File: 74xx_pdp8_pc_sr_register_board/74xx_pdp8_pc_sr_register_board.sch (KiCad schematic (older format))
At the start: 33 parts, among them P1 DIL24, P2 DIL24, P3 DIL24, P4 DIL24, P5 DIL24, U1 74HC125, U10 74HC04, U11 74HC163, U12 74HC163, U13 74HC163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

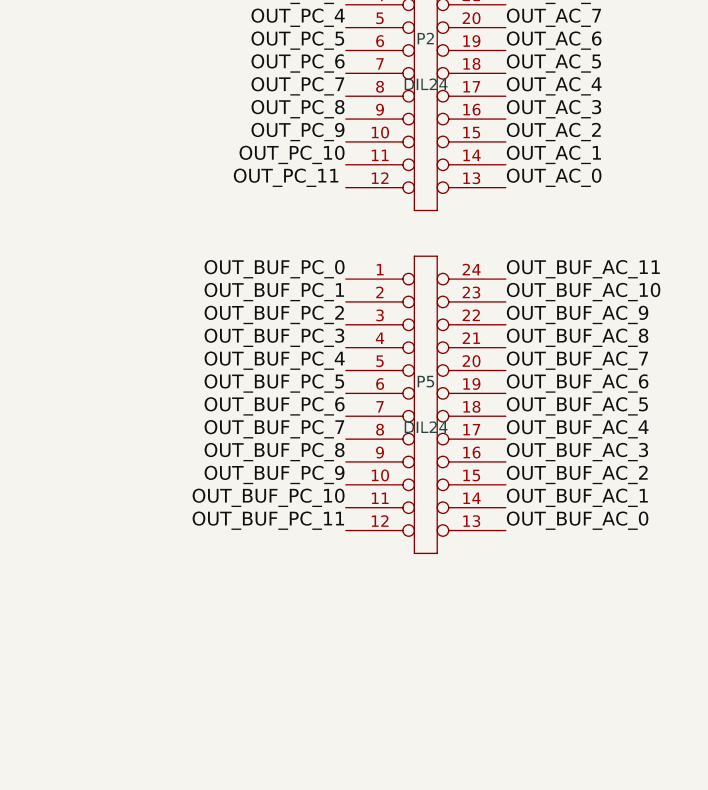
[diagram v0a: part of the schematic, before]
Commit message: Big changes - elected to switch to board interconnections along one long edge only. Boards to connect to backplane via right-angled DIL connectors. Both register boards and register mux boards thusly modified.
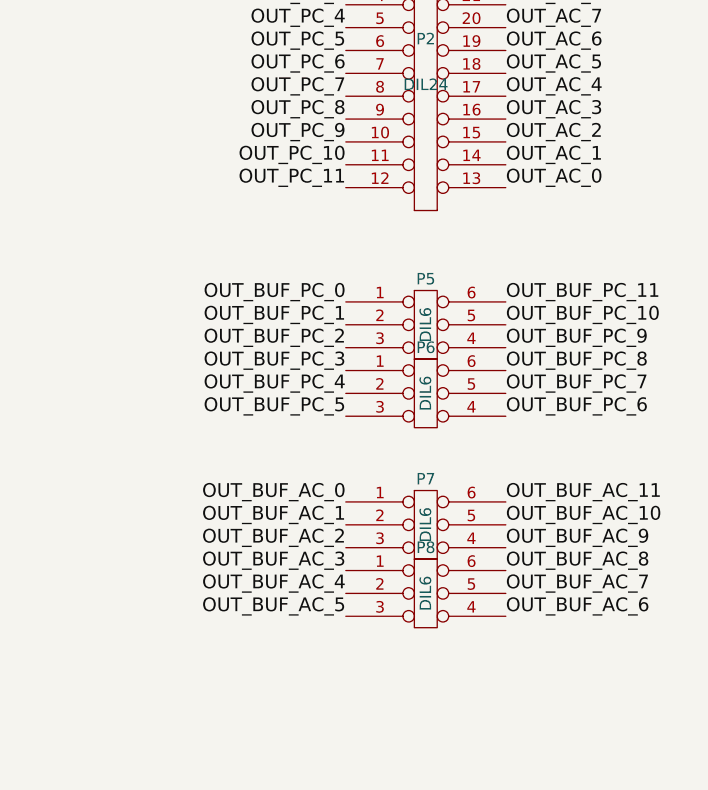
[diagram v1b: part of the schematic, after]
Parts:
- removed P5: DIL24, Socket_Strips:Socket_Strip_Straight_2x12, symbol DIL24
- added P5, P6, P7, P8: DIL6, Socket_Strips:Socket_Strip_Straight_2x03, symbol DIL6
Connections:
- net OUT_BUF_AC_0: now also P7.1 (P1)
- net OUT_BUF_AC_1: now also P7.2 (P2)
- net OUT_BUF_AC_10: now also P7.5 (P5)
- net OUT_BUF_AC_11: now also P7.6 (P6)
- net OUT_BUF_AC_2: now also P7.3 (P3)
- net OUT_BUF_AC_3: now also P8.1 (P1)
- net OUT_BUF_AC_4: now also P8.2 (P2)
- net OUT_BUF_AC_5: now also P8.3 (P3)
- net OUT_BUF_AC_6: now also P8.4 (P4)
- net OUT_BUF_AC_7: now also P8.5 (P5)
- net OUT_BUF_AC_8: now also P8.6 (P6)
- net OUT_BUF_AC_9: now also P7.4 (P4)
- net OUT_BUF_PC_0: now also P5.1 (P1)
- net OUT_BUF_PC_1: now also P5.2 (P2)
- net OUT_BUF_PC_10: now also P5.5 (P5)
- net OUT_BUF_PC_11: now also P5.6 (P6)
- net OUT_BUF_PC_2: now also P5.3 (P3)
- net OUT_BUF_PC_3: now also P6.1 (P1)
- net OUT_BUF_PC_4: now also P6.2 (P2)
- net OUT_BUF_PC_5: now also P6.3 (P3)
- net OUT_BUF_PC_6: now also P6.4 (P4)
- net OUT_BUF_PC_7: now also P6.5 (P5)
- net OUT_BUF_PC_8: now also P6.6 (P6)
- net OUT_BUF_PC_9: now also P5.4 (P4)
- net OUT_PC_11: now also P2.12 (P12)
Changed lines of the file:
@@
 Text Label 2450 3600 2    60   ~ 0
 CLK
-$Comp
-L DIL24 P5
-U 1 1 5AC9104A
-P 19075 5250
-F 0 "P5" H 19075 5350 50  0000 C CNN
-F 1 "DIL24" H 19075 5150 50  0000 C CNN
-F 2 "Socket_Strips:Socket_Strip_Straight_2x12" H 19075 5250 50  0001 C CNN
-F 3 "" H 19075 5250 50  0000 C CNN
-	1    19075 5250
-	1    0    0    -1
-$EndComp
 Text Label 2450 3700 2    60   ~ 0
 LOAD_HI_MA
@@
 Text Label 14825 8525 1    60   ~ 0
 OUT_AC_6
+Text Label 18725 4900 2    60   ~ 0
+OUT_BUF_PC_1
+Text Label 18725 5000 2    60   ~ 0
+OUT_BUF_PC_2
+Text Label 18725 5100 2    60   ~ 0
+OUT_BUF_PC_3
+Text Label 18725 5200 2    60   ~ 0
+OUT_BUF_PC_4
+Text Label 18725 5300 2    60   ~ 0
+OUT_BUF_PC_5
+Text Label 19425 5300 0    60   ~ 0
+OUT_BUF_PC_6
+Text Label 19425 5200 0    60   ~ 0
+OUT_BUF_PC_7
+Text Label 19425 5100 0    60   ~ 0
+OUT_BUF_PC_8
+Text Label 19425 5000 0    60   ~ 0
+OUT_BUF_PC_9
+Text Label 19425 4900 0    60   ~ 0
+OUT_BUF_PC_10
+Text Label 19425 4800 0    60   ~ 0
+OUT_BUF_PC_11
 Text Label 18725 4800 2    60   ~ 0
-OUT_BUF_PC_1
-Text Label 18725 4900 2    60   ~ 0
-OUT_BUF_PC_2
-Text Label 18725 5000 2    60   ~ 0
-OUT_BUF_PC_3
-Text Label 18725 5100 2    60   ~ 0
-OUT_BUF_PC_4
-Text Label 18725 5200 2    60   ~ 0
-OUT_BUF_PC_5
-Text Label 18725 5300 2    60   ~ 0
-OUT_BUF_PC_6
-Text Label 18725 5400 2    60   ~ 0
-OUT_BUF_PC_7
-Text Label 18725 5500 2    60   ~ 0
-OUT_BUF_PC_8
-Text Label 18725 5600 2    60   ~ 0
-OUT_BUF_PC_9
-Text Label 18725 5700 2    60   ~ 0
-OUT_BUF_PC_10
-Text Label 18725 5800 2    60   ~ 0
-OUT_BUF_PC_11
-Text Label 18725 4700 2    60   ~ 0
 OUT_BUF_PC_0
 Text Label 18725 3200 2    60   ~ 0
@@
 Text Label 18725 4200 2    60   ~ 0
 OUT_PC_10
-Text Label 18700 4300 2    60   ~ 0
+Text Label 18725 4300 2    60   ~ 0
 OUT_PC_11
 $Comp
@@
 Text Label 19425 3200 0    60   ~ 0
 OUT_AC_11
-Text Label 19425 5800 0    60   ~ 0
+Text Label 18725 5675 2    60   ~ 0
 OUT_BUF_AC_0
-Text Label 19425 5700 0    60   ~ 0
+Text Label 18725 5775 2    60   ~ 0
 OUT_BUF_AC_1
-Text Label 19425 5600 0    60   ~ 0
+Text Label 18725 5875 2    60   ~ 0
 OUT_BUF_AC_2
-Text Label 19425 5500 0    60   ~ 0
+Text Label 18725 5975 2    60   ~ 0
 OUT_BUF_AC_3
-Text Label 19425 5400 0    60   ~ 0
+Text Label 18725 6075 2    60   ~ 0
 OUT_BUF_AC_4
-Text Label 19425 5300 0    60   ~ 0
+Text Label 18725 6175 2    60   ~ 0
 OUT_BUF_AC_5
-Text Label 19425 5200 0    60   ~ 0
+Text Label 19425 6175 0    60   ~ 0
 OUT_BUF_AC_6
-Text Label 19425 5100 0    60   ~ 0
+Text Label 19425 6075 0    60   ~ 0
 OUT_BUF_AC_7
-Text Label 19425 5000 0    60   ~ 0
+Text Label 19425 5975 0    60   ~ 0
 OUT_BUF_AC_8
-Text Label 19425 4900 0    60   ~ 0
+Text Label 19425 5875 0    60   ~ 0
 OUT_BUF_AC_9
-Text Label 19425 4800 0    60   ~ 0
+Text Label 19425 5775 0    60   ~ 0
 OUT_BUF_AC_10
-Text Label 19425 4700 0    60   ~ 0
+Text Label 19425 5675 0    60   ~ 0
 OUT_BUF_AC_11
+$Comp
+L DIL6 P5
+U 1 1 5AC94B8F
+P 19075 4900
+F 0 "P5" H 19075 5100 50  0000 C CNN
+F 1 "DIL6" V 19075 4900 50  0000 C CNN
+F 2 "Socket_Strips:Socket_Strip_Straight_2x03" H 19075 4900 50  0001 C CNN
+F 3 "" H 19075 4900 50  0000 C CNN
+	1    19075 4900
+	1    0    0    -1
+$EndComp
+$Comp
+L DIL6 P6
+U 1 1 5AC94E2C
+P 19075 5200
+F 0 "P6" H 19075 5400 50  0000 C CNN
+F 1 "DIL6" V 19075 5200 50  0000 C CNN
+F 2 "Socket_Strips:Socket_Strip_Straight_2x03" H 19075 5200 50  0001 C CNN
+F 3 "" H 19075 5200 50  0000 C CNN
+	1    19075 5200
+	1    0    0    -1
+$EndComp
+$Comp
+L DIL6 P7
+U 1 1 5AC94ED5
+P 19075 5775
+F 0 "P7" H 19075 5975 50  0000 C CNN
+F 1 "DIL6" V 19075 5775 50  0000 C CNN
+F 2 "Socket_Strips:Socket_Strip_Straight_2x03" H 19075 5775 50  0001 C CNN
+F 3 "" H 19075 5775 50  0000 C CNN
+	1    19075 5775
+	1    0    0    -1
+$EndComp
+$Comp
+L DIL6 P8
+U 1 1 5AC94FD0
+P 19075 6075
+F 0 "P8" H 19075 6275 50  0000 C CNN
+F 1 "DIL6" V 19075 6075 50  0000 C CNN
+F 2 "Socket_Strips:Socket_Strip_Straight_2x03" H 19075 6075 50  0001 C CNN
+F 3 "" H 19075 6075 50  0000 C CNN
+	1    19075 6075
+	1    0    0    -1
+$EndComp
 $EndSCHEMATC
